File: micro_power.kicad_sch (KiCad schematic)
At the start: 25 parts

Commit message: major progress with memory interfacing
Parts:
- removed D?: WP424NDT, symbol tbc:WP424NDT
- removed R?: 560, symbol tbc:RC0603FR-07560RL
- added R?: 10k, symbol tbc:RC0603FR-0710KL
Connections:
- net +3V3: now also R?.2
- net GND: no longer J?.5
- net at C?.2, J?.10, SW?.3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: now also R?.1
- new net FREEZE: J?.5
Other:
- note added: "Power"
- moved on the sheet: C?, J?, Q?, R?, SW?, U?, Y?

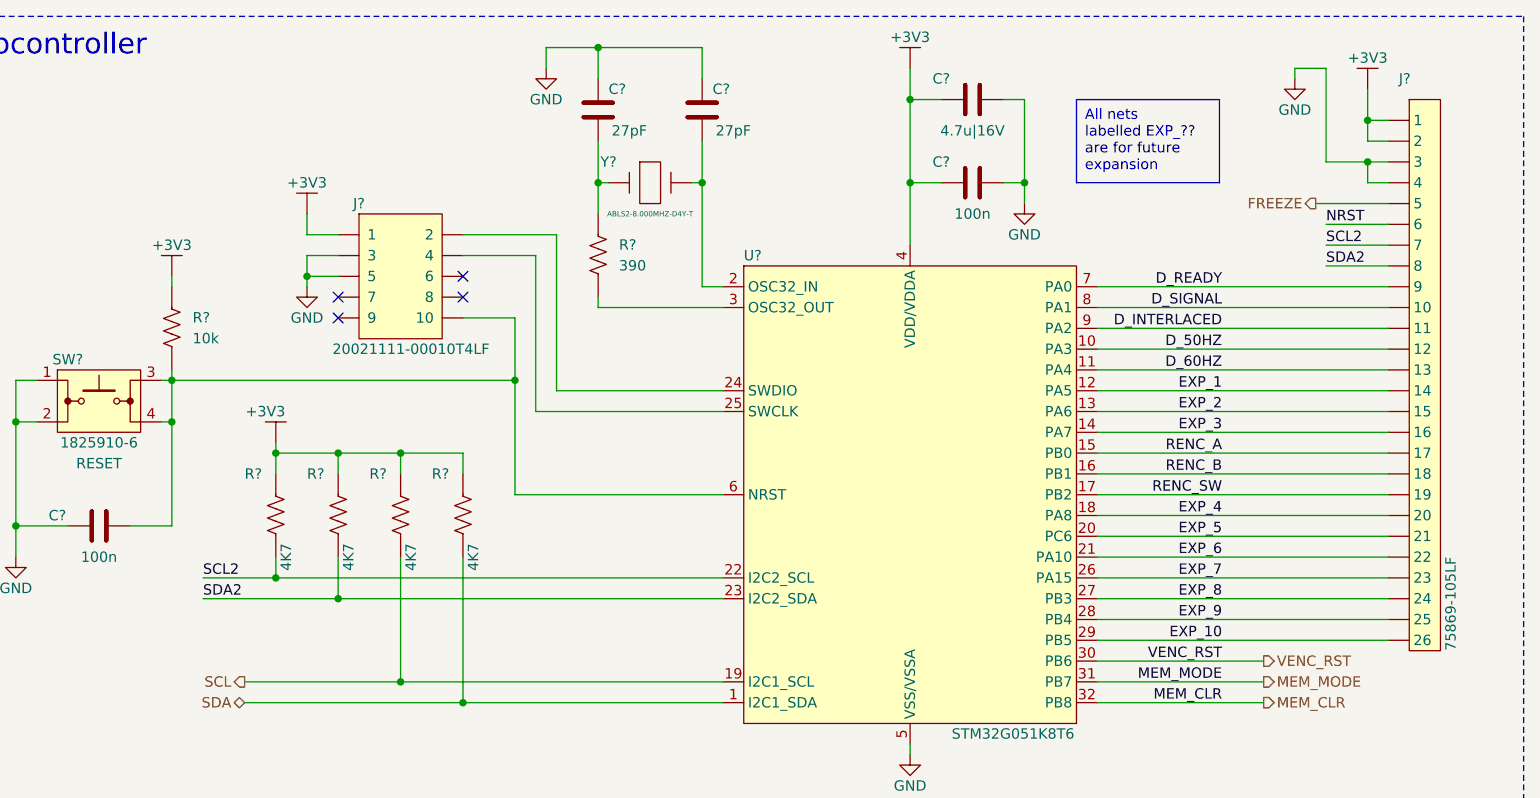
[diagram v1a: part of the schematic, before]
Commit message: minor changes to schematic layout
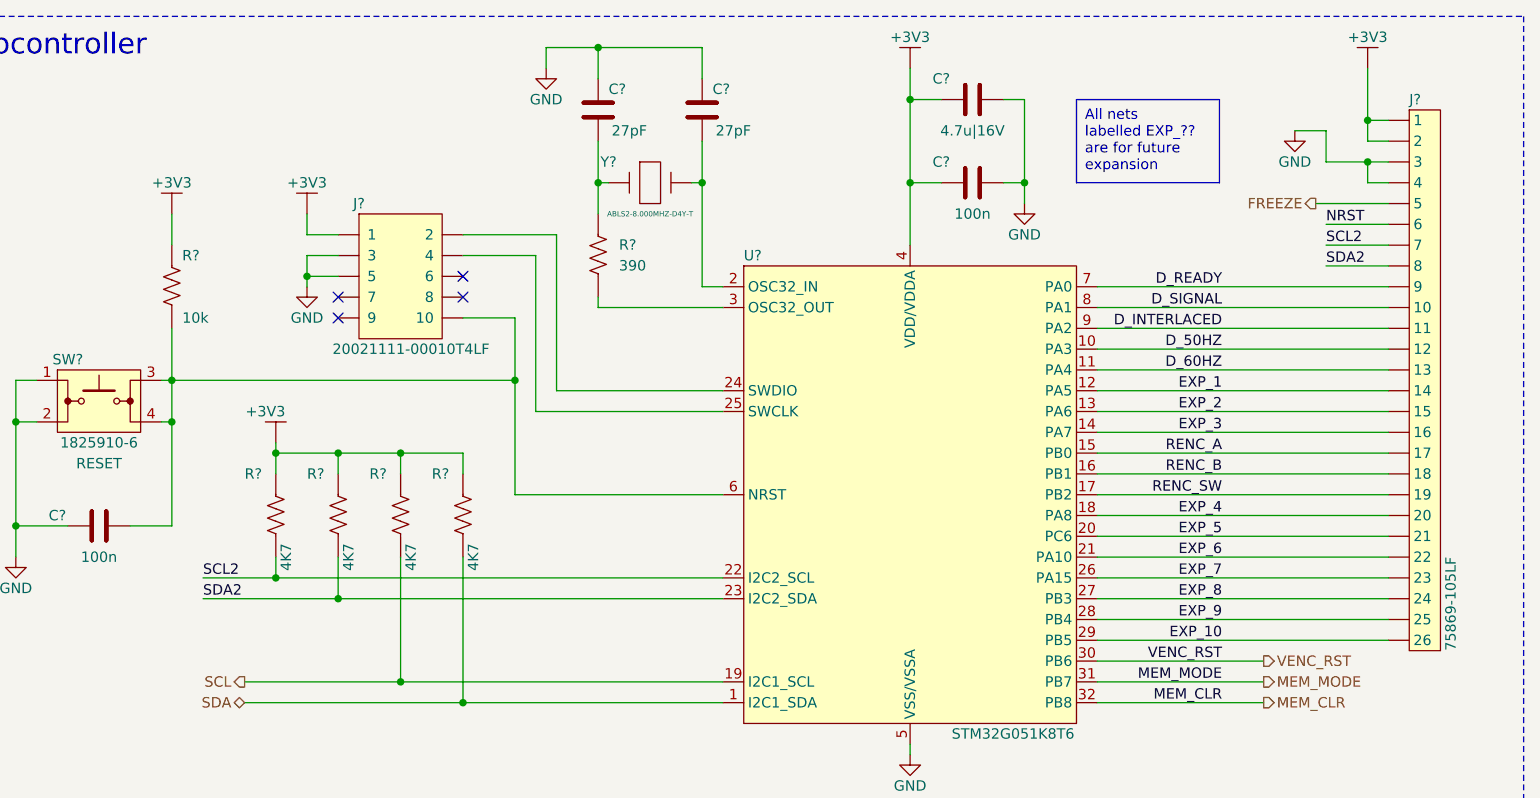
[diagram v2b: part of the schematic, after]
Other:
- moved on the sheet: J?, R?
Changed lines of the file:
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@@
     (stroke (width 0) (type default))
   )
-  (wire (pts (xy 217.17 40.64) (xy 212.09 40.64))
+  (wire (pts (xy 212.09 40.64) (xy 217.17 40.64))
     (stroke (width 0) (type default))
   )
@@
     (stroke (width 0) (type default))
   )
-  (wire (pts (xy 71.12 66.04) (xy 71.12 67.31))
+  (wire (pts (xy 212.09 36.83) (xy 208.28 36.83))
+    (stroke (width 0) (type default))
+  )
+  (wire (pts (xy 71.12 60.96) (xy 71.12 67.31))
     (stroke (width 0) (type default))
   )
@@
     (stroke (width 0) (type default))
   )
+  (wire (pts (xy 212.09 36.83) (xy 212.09 40.64))
+    (stroke (width 0) (type default))
+  )
   (wire (pts (xy 106.68 153.67) (xy 106.68 162.56))
     (stroke (width 0) (type default))
@@
     (stroke (width 0) (type default))
   )
-  (wire (pts (xy 212.09 40.64) (xy 212.09 29.21))
-    (stroke (width 0) (type default))
-  )
   (wire (pts (xy 119.38 139.7) (xy 121.92 139.7))
     (stroke (width 0) (type default))
@@
     (stroke (width 0) (type default))
   )
-  (wire (pts (xy 71.12 54.61) (xy 71.12 55.88))
+  (wire (pts (xy 71.12 46.99) (xy 71.12 50.8))
     (stroke (width 0) (type default))
   )
@@
     (stroke (width 0) (type default))
   )
-  (wire (pts (xy 217.17 35.56) (xy 217.17 31.75))
+  (wire (pts (xy 217.17 35.56) (xy 217.17 29.21))
     (stroke (width 0) (type default))
   )
@@
     (stroke (width 0) (type default))
   )
-  (wire (pts (xy 212.09 29.21) (xy 208.28 29.21))
-    (stroke (width 0) (type default))
-  )
   (wire (pts (xy 210.82 45.72) (xy 219.71 45.72))
     (stroke (width 0) (type default))
@@
   )
   (wire (pts (xy 83.82 88.9) (xy 83.82 91.44))
-    (stroke (width 0) (type default))
-  )
-  (wire (pts (xy 208.28 29.21) (xy 208.28 30.48))
     (stroke (width 0) (type default))
   )
@@
     )
   )
-  (symbol (lib_id "tbc:+3V3") (at 71.12 54.61 0) (unit 1)
-    (in_bom yes) (on_board yes) (dnp no)
-    (property "Reference" "#PWR048" (at 71.12 64.77 0)
-      (effects (font (size 1.27 1.27)) hide)
-    )
-    (property "Value" "+3V3" (at 71.12 50.8 0)
-      (effects (font (size 1.27 1.27)))
-    )
-    (property "Footprint" "" (at 71.12 54.61 0)
-      (effects (font (size 1.27 1.27)) hide)
-    )
-    (property "Datasheet" "" (at 71.12 54.61 0)
+  (symbol (lib_id "tbc:+3V3") (at 71.12 46.99 0) (unit 1)
+    (in_bom yes) (on_board yes) (dnp no)
+    (property "Reference" "#PWR048" (at 71.12 57.15 0)
+      (effects (font (size 1.27 1.27)) hide)
+    )
+    (property "Value" "+3V3" (at 71.12 43.18 0)
+      (effects (font (size 1.27 1.27)))
+    )
+    (property "Footprint" "" (at 71.12 46.99 0)
+      (effects (font (size 1.27 1.27)) hide)
+    )
+    (property "Datasheet" "" (at 71.12 46.99 0)
       (effects (font (size 1.27 1.27)) hide)
     )
@@
     )
   )
-  (symbol (lib_id "tbc:+3V3") (at 217.17 31.75 0) (unit 1)
-    (in_bom yes) (on_board yes) (dnp no)
-    (property "Reference" "#PWR025" (at 217.17 41.91 0)
-      (effects (font (size 1.27 1.27)) hide)
-    )
-    (property "Value" "+3V3" (at 217.17 27.94 0)
-      (effects (font (size 1.27 1.27)))
-    )
-    (property "Footprint" "" (at 217.17 31.75 0)
-      (effects (font (size 1.27 1.27)) hide)
-    )
-    (property "Datasheet" "" (at 217.17 31.75 0)
+  (symbol (lib_id "tbc:+3V3") (at 217.17 29.21 0) (unit 1)
+    (in_bom yes) (on_board yes) (dnp no)
+    (property "Reference" "#PWR025" (at 217.17 39.37 0)
+      (effects (font (size 1.27 1.27)) hide)
+    )
+    (property "Value" "+3V3" (at 217.17 25.4 0)
+      (effects (font (size 1.27 1.27)))
+    )
+    (property "Footprint" "" (at 217.17 29.21 0)
+      (effects (font (size 1.27 1.27)) hide)
+    )
+    (property "Datasheet" "" (at 217.17 29.21 0)
       (effects (font (size 1.27 1.27)) hide)
     )
@@
     )
   )
-  (symbol (lib_id "tbc:GND") (at 208.28 30.48 0) (unit 1)
-    (in_bom yes) (on_board yes) (dnp no)
-    (property "Reference" "#PWR027" (at 208.28 36.83 0)
-      (effects (font (size 1.27 1.27)) hide)
-    )
-    (property "Value" "GND" (at 208.28 34.29 0)
-      (effects (font (size 1.27 1.27)))
-    )
-    (property "Footprint" "" (at 208.28 30.48 0)
-      (effects (font (size 1.27 1.27)) hide)
-    )
-    (property "Datasheet" "" (at 208.28 30.48 0)
+  (symbol (lib_id "tbc:GND") (at 208.28 36.83 0) (unit 1)
+    (in_bom yes) (on_board yes) (dnp no)
+    (property "Reference" "#PWR027" (at 208.28 43.18 0)
+      (effects (font (size 1.27 1.27)) hide)
+    )
+    (property "Value" "GND" (at 208.28 40.64 0)
+      (effects (font (size 1.27 1.27)))
+    )
+    (property "Footprint" "" (at 208.28 36.83 0)
+      (effects (font (size 1.27 1.27)) hide)
+    )
+    (property "Datasheet" "" (at 208.28 36.83 0)
       (effects (font (size 1.27 1.27)) hide)
     )
@@
     )
   )
-  (symbol (lib_id "tbc:RC0603FR-0710KL") (at 71.12 60.96 90) (unit 1)
-    (in_bom yes) (on_board yes) (dnp no) (fields_autoplaced)
-    (property "Reference" "R?" (at 73.66 59.6582 90)
+  (symbol (lib_id "tbc:RC0603FR-0710KL") (at 71.12 55.88 90) (unit 1)
+    (in_bom yes) (on_board yes) (dnp no)
+    (property "Reference" "R?" (at 72.39 52.07 90)
       (effects (font (size 1.27 1.27)) (justify right))
     )
-    (property "Value" "10k" (at 73.66 62.1982 90)
+    (property "Value" "10k" (at 72.39 59.69 90)
       (effects (font (size 1.27 1.27)) (justify right))
     )
-    (property "Footprint" "" (at 78.74 77.47 0)
-      (effects (font (size 1.27 1.27)) hide)
-    )
-    (property "Datasheet" "https://www.mouser.com/datasheet/2/447/YAGEO_PYu_RC_Group_51_RoHS_L_12-3313492.pdf" (at 83.82 77.47 0) (show_name)
-      (effects (font (size 1.27 1.27)) (justify left) hide)
-    )
-    (property "Mouser" "603-RC0603FR-0710KL" (at 81.28 77.47 0) (show_name)
+    (property "Footprint" "" (at 78.74 72.39 0)
+      (effects (font (size 1.27 1.27)) hide)
+    )
+    (property "Datasheet" "https://www.mouser.com/datasheet/2/447/YAGEO_PYu_RC_Group_51_RoHS_L_12-3313492.pdf" (at 83.82 72.39 0) (show_name)
+      (effects (font (size 1.27 1.27)) (justify left) hide)
+    )
+    (property "Mouser" "603-RC0603FR-0710KL" (at 81.28 72.39 0) (show_name)
       (effects (font (size 1.27 1.27)) (justify left) hide)
     )
@@
   (symbol (lib_id "tbc:75869-105LF") (at 222.25 66.04 0) (unit 1)
     (in_bom yes) (on_board yes) (dnp no)
-    (property "Reference" "J?" (at 220.98 30.48 0)
+    (property "Reference" "J?" (at 222.25 33.02 0)
       (effects (font (size 1.27 1.27)) (justify left))
     )
